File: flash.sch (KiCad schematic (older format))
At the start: 6 parts, among them U1901 MX25L1606E

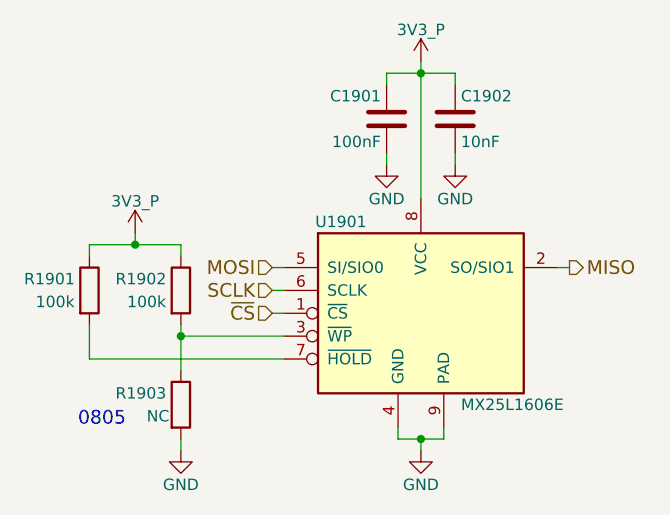
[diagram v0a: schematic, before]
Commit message: Add MIPI CSI sheet (contents need to be added once camera selection is complete)
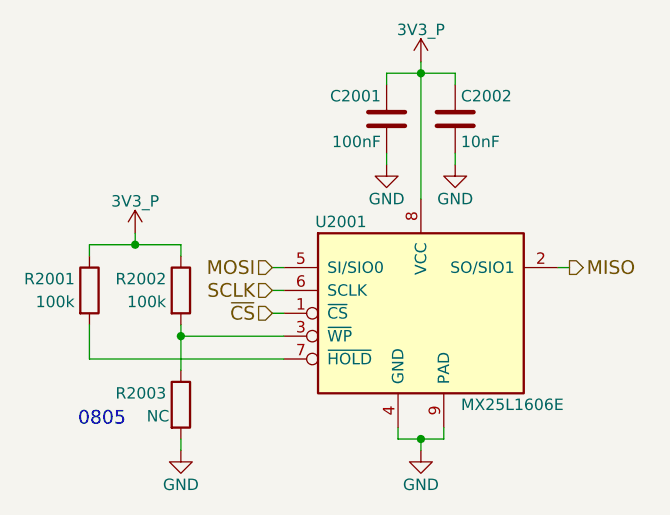
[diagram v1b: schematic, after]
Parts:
- renumbered C1901 to C2001, C1902 to C2002, R1901 to R2001, R1902 to R2002, R1903 to R2003, U1901 to U2001
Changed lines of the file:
@@
 $Descr A4 11693 8268
 encoding utf-8
-Sheet 20 20
+Sheet 20 21
 Title "SPI NOR Flash"
 Date "2018-05-18"
@@
 $EndDescr
 $Comp
-L GND #PWR0318
+L GND #PWR2005
 U 1 1 5B12CD29
 P 6000 4300
-F 0 "#PWR0318" H 6000 4050 50  0001 C CNN
+F 0 "#PWR2005" H 6000 4050 50  0001 C CNN
 F 1 "GND" H 6000 4150 50  0000 C CNN
 F 2 "" H 6000 4300 50  0001 C CNN
@@
 $EndComp
 $Comp
-L MX25L1606E U1901
+L MX25L1606E U2001
 U 1 1 5B12CFC8
 P 6000 3700
-F 0 "U1901" H 5650 4100 50  0000 C CNN
+F 0 "U2001" H 5650 4100 50  0000 C CNN
 F 1 "MX25L1606E" H 6400 3300 50  0000 C CNN
 F 2 "Housings_DFN_QFN:DFN-S-8-1EP_6x5mm_Pitch1.27mm" H 6800 3800 50  0001 C CNN
@@
 $EndComp
 $Comp
-L 3V3_P #PWR0319
+L 3V3_P #PWR2004
 U 1 1 5B12EA15
 P 6000 2600
-F 0 "#PWR0319" H 6000 2450 50  0001 C CNN
+F 0 "#PWR2004" H 6000 2450 50  0001 C CNN
 F 1 "3V3_P" H 6000 2740 50  0000 C CNN
 F 2 "" H 6000 2600 50  0001 C CNN
@@
 $EndComp
 $Comp
-L C C1901
+L C C2001
 U 1 1 5B12EA2B
 P 5850 2850
-F 0 "C1901" H 5875 2950 50  0000 L CNN
+F 0 "C2001" H 5875 2950 50  0000 L CNN
 F 1 "100nF" H 5875 2750 50  0000 L CNN
 F 2 "" H 5888 2700 50  0001 C CNN
@@
 $EndComp
 $Comp
-L C C1902
+L C C2002
 U 1 1 5B14E905
 P 6150 2850
-F 0 "C1902" H 6175 2950 50  0000 L CNN
+F 0 "C2002" H 6175 2950 50  0000 L CNN
 F 1 "10nF" H 6175 2750 50  0000 L CNN
 F 2 "" H 6188 2700 50  0001 C CNN
@@
 $EndComp
 $Comp
-L GND #PWR0320
+L GND #PWR2003
 U 1 1 5B14F686
 P 5850 3050
-F 0 "#PWR0320" H 5850 2800 50  0001 C CNN
+F 0 "#PWR2003" H 5850 2800 50  0001 C CNN
 F 1 "GND" H 5850 2900 50  0000 C CNN
 F 2 "" H 5850 3050 50  0001 C CNN
@@
 $EndComp
 $Comp
-L GND #PWR0321
+L GND #PWR2006
 U 1 1 5B14F6A1
 P 6150 3050
-F 0 "#PWR0321" H 6150 2800 50  0001 C CNN
+F 0 "#PWR2006" H 6150 2800 50  0001 C CNN
 F 1 "GND" H 6150 2900 50  0000 C CNN
 F 2 "" H 6150 3050 50  0001 C CNN
@@
 ~CS
 $Comp
-L R R1901
+L R R2001
 U 1 1 5B152CDF
 P 4550 3600
-F 0 "R1901" H 4375 3650 50  0000 C CNN
+F 0 "R2001" H 4375 3650 50  0000 C CNN
 F 1 "100k" H 4400 3550 50  0000 C CNN
 F 2 "" V 4480 3600 50  0001 C CNN
@@
 $EndComp
 $Comp
-L 3V3_P #PWR0322
+L 3V3_P #PWR2001
 U 1 1 5B152DB7
 P 4750 3350
-F 0 "#PWR0322" H 4750 3200 50  0001 C CNN
+F 0 "#PWR2001" H 4750 3200 50  0001 C CNN
 F 1 "3V3_P" H 4750 3490 50  0000 C CNN
 F 2 "" H 4750 3350 50  0001 C CNN
@@
 $EndComp
 $Comp
-L R R1902
+L R R2002
 U 1 1 5AFB92E3
 P 4950 3600
-F 0 "R1902" H 4775 3650 50  0000 C CNN
+F 0 "R2002" H 4775 3650 50  0000 C CNN
 F 1 "100k" H 4800 3550 50  0000 C CNN
 F 2 "" V 4880 3600 50  0001 C CNN
@@
 $EndComp
 $Comp
-L R R1903
+L R R2003
 U 1 1 5AFBA0EE
 P 4950 4100
-F 0 "R1903" H 4775 4150 50  0000 C CNN
+F 0 "R2003" H 4775 4150 50  0000 C CNN
 F 1 "NC" H 4850 4050 50  0000 C CNN
 F 2 "" V 4880 4100 50  0001 C CNN
@@
 Connection ~ 4950 3800
 $Comp
-L GND #PWR0323
+L GND #PWR2002
 U 1 1 5AFBA2C4
 P 4950 4300
-F 0 "#PWR0323" H 4950 4050 50  0001 C CNN
+F 0 "#PWR2002" H 4950 4050 50  0001 C CNN
 F 1 "GND" H 4950 4150 50  0000 C CNN
 F 2 "" H 4950 4300 50  0001 C CNN

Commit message: Begin assigning footprints to passive components, add component information to the common 10k resistors throughout the schematic, include TVS diodes on the switch/button I/O pins, use the DB2J20900L schottky diode throughout the design (in place of the ZLLS400)
Added notes about the battery holder, battery size, and the fact that the 103HT thermistor can fit underneath the 18650 battery when the battery is insterted into the holder.

Included frequency response curve for the new/cheaper SMD speaker (slightly thicker mechanical dimension).

Included note about the RedPine RS9116's SDIO_RESET# line expecting a 2.31V VIH logic level, increased the pull-up to 100k (M.2 standard states that this is should be 1.8V level).

Added a TODO note stating the 1.8V logic-level I2C devices should share the same level-shifter that will be on the top-level circuit (in next commit).
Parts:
- R2001, R2002, R2003: footprint (none) -> Resistors_SMD:R_0603
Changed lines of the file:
@@
 $EndDescr
 $Comp
-L GND #PWR2005
+L GND #PWR0324
 U 1 1 5B12CD29
 P 6000 4300
-F 0 "#PWR2005" H 6000 4050 50  0001 C CNN
+F 0 "#PWR0324" H 6000 4050 50  0001 C CNN
 F 1 "GND" H 6000 4150 50  0000 C CNN
 F 2 "" H 6000 4300 50  0001 C CNN
@@
 $EndComp
 $Comp
-L 3V3_P #PWR2004
+L 3V3_P #PWR0325
 U 1 1 5B12EA15
 P 6000 2600
-F 0 "#PWR2004" H 6000 2450 50  0001 C CNN
+F 0 "#PWR0325" H 6000 2450 50  0001 C CNN
 F 1 "3V3_P" H 6000 2740 50  0000 C CNN
 F 2 "" H 6000 2600 50  0001 C CNN
@@
 $EndComp
 $Comp
-L GND #PWR2003
+L GND #PWR0326
 U 1 1 5B14F686
 P 5850 3050
-F 0 "#PWR2003" H 5850 2800 50  0001 C CNN
+F 0 "#PWR0326" H 5850 2800 50  0001 C CNN
 F 1 "GND" H 5850 2900 50  0000 C CNN
 F 2 "" H 5850 3050 50  0001 C CNN
@@
 $EndComp
 $Comp
-L GND #PWR2006
+L GND #PWR0327
 U 1 1 5B14F6A1
 P 6150 3050
-F 0 "#PWR2006" H 6150 2800 50  0001 C CNN
+F 0 "#PWR0327" H 6150 2800 50  0001 C CNN
 F 1 "GND" H 6150 2900 50  0000 C CNN
 F 2 "" H 6150 3050 50  0001 C CNN
@@
 F 0 "R2001" H 4375 3650 50  0000 C CNN
 F 1 "100k" H 4400 3550 50  0000 C CNN
-F 2 "" V 4480 3600 50  0001 C CNN
+F 2 "Resistors_SMD:R_0603" V 4480 3600 50  0001 C CNN
 F 3 "" H 4550 3600 50  0001 C CNN
 	1    4550 3600
@@
 $EndComp
 $Comp
-L 3V3_P #PWR2001
+L 3V3_P #PWR0328
 U 1 1 5B152DB7
 P 4750 3350
-F 0 "#PWR2001" H 4750 3200 50  0001 C CNN
+F 0 "#PWR0328" H 4750 3200 50  0001 C CNN
 F 1 "3V3_P" H 4750 3490 50  0000 C CNN
 F 2 "" H 4750 3350 50  0001 C CNN
@@
 F 0 "R2002" H 4775 3650 50  0000 C CNN
 F 1 "100k" H 4800 3550 50  0000 C CNN
-F 2 "" V 4880 3600 50  0001 C CNN
+F 2 "Resistors_SMD:R_0603" V 4880 3600 50  0001 C CNN
 F 3 "" H 4950 3600 50  0001 C CNN
 	1    4950 3600
@@
 F 0 "R2003" H 4775 4150 50  0000 C CNN
 F 1 "NC" H 4850 4050 50  0000 C CNN
-F 2 "" V 4880 4100 50  0001 C CNN
+F 2 "Resistors_SMD:R_0603" V 4880 4100 50  0001 C CNN
 F 3 "" H 4950 4100 50  0001 C CNN
 	1    4950 4100
@@
 Connection ~ 4950 3800
 $Comp
-L GND #PWR2002
+L GND #PWR0329
 U 1 1 5AFBA2C4
 P 4950 4300
-F 0 "#PWR2002" H 4950 4050 50  0001 C CNN
+F 0 "#PWR0329" H 4950 4050 50  0001 C CNN
 F 1 "GND" H 4950 4150 50  0000 C CNN
 F 2 "" H 4950 4300 50  0001 C CNN

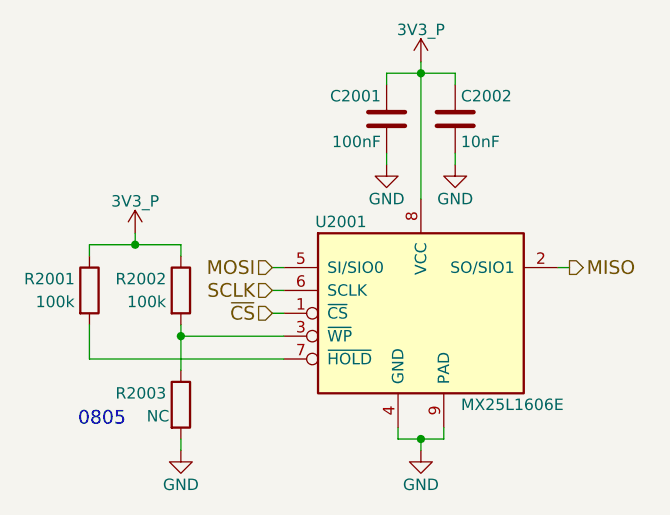
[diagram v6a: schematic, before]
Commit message: Modify the boot config/boot mode pins and switch such that only eMMC and USB (serial downloader) are boot options due to the uSD being attached to the USB<->SD bridge chip, add OV5460 notes about using the internal DVDD 1.5V regulator
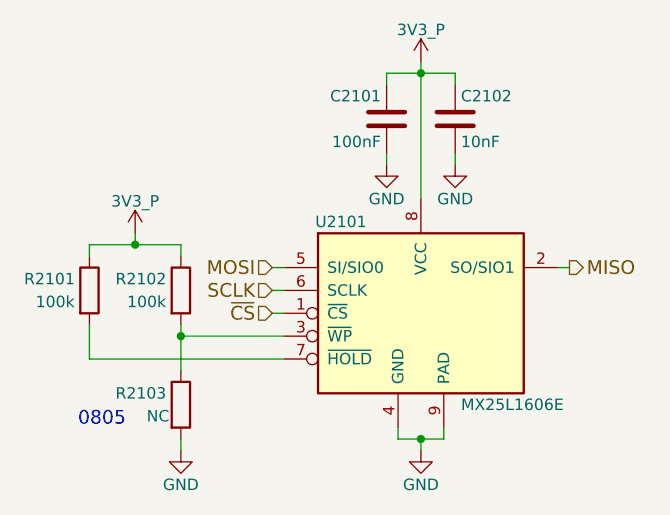
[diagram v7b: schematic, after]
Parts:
- renumbered C2001 to C2101, C2002 to C2102, R2001 to R2101, R2002 to R2102, R2003 to R2103, U2001 to U2101
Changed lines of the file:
@@
 $EndDescr
 $Comp
-L GND #PWR0327
+L GND #PWR0321
 U 1 1 5B12CD29
 P 6000 4300
-F 0 "#PWR0327" H 6000 4050 50  0001 C CNN
+F 0 "#PWR0321" H 6000 4050 50  0001 C CNN
 F 1 "GND" H 6000 4150 50  0000 C CNN
 F 2 "" H 6000 4300 50  0001 C CNN
@@
 $EndComp
 $Comp
-L MX25L1606E U2001
+L MX25L1606E U2101
 U 1 1 5B12CFC8
 P 6000 3700
-F 0 "U2001" H 5650 4100 50  0000 C CNN
+F 0 "U2101" H 5650 4100 50  0000 C CNN
 F 1 "MX25L1606E" H 6400 3300 50  0000 C CNN
 F 2 "Housings_DFN_QFN:DFN-S-8-1EP_6x5mm_Pitch1.27mm" H 6800 3800 50  0001 C CNN
@@
 $EndComp
 $Comp
-L 3V3_P #PWR0328
+L 3V3_P #PWR0322
 U 1 1 5B12EA15
 P 6000 2600
-F 0 "#PWR0328" H 6000 2450 50  0001 C CNN
+F 0 "#PWR0322" H 6000 2450 50  0001 C CNN
 F 1 "3V3_P" H 6000 2740 50  0000 C CNN
 F 2 "" H 6000 2600 50  0001 C CNN
@@
 $EndComp
 $Comp
-L C C2001
+L C C2101
 U 1 1 5B12EA2B
 P 5850 2850
-F 0 "C2001" H 5875 2950 50  0000 L CNN
+F 0 "C2101" H 5875 2950 50  0000 L CNN
 F 1 "100nF" H 5875 2750 50  0000 L CNN
 F 2 "" H 5888 2700 50  0001 C CNN
@@
 $EndComp
 $Comp
-L C C2002
+L C C2102
 U 1 1 5B14E905
 P 6150 2850
-F 0 "C2002" H 6175 2950 50  0000 L CNN
+F 0 "C2102" H 6175 2950 50  0000 L CNN
 F 1 "10nF" H 6175 2750 50  0000 L CNN
 F 2 "" H 6188 2700 50  0001 C CNN
@@
 $EndComp
 $Comp
-L GND #PWR0329
+L GND #PWR0323
 U 1 1 5B14F686
 P 5850 3050
-F 0 "#PWR0329" H 5850 2800 50  0001 C CNN
+F 0 "#PWR0323" H 5850 2800 50  0001 C CNN
 F 1 "GND" H 5850 2900 50  0000 C CNN
 F 2 "" H 5850 3050 50  0001 C CNN
@@
 $EndComp
 $Comp
-L GND #PWR0330
+L GND #PWR0324
 U 1 1 5B14F6A1
 P 6150 3050
-F 0 "#PWR0330" H 6150 2800 50  0001 C CNN
+F 0 "#PWR0324" H 6150 2800 50  0001 C CNN
 F 1 "GND" H 6150 2900 50  0000 C CNN
 F 2 "" H 6150 3050 50  0001 C CNN
@@
 ~CS
 $Comp
-L R R2001
+L R R2101
 U 1 1 5B152CDF
 P 4550 3600
-F 0 "R2001" H 4375 3650 50  0000 C CNN
+F 0 "R2101" H 4375 3650 50  0000 C CNN
 F 1 "100k" H 4400 3550 50  0000 C CNN
 F 2 "Resistors_SMD:R_0603" V 4480 3600 50  0001 C CNN
@@
 $EndComp
 $Comp
-L 3V3_P #PWR0331
+L 3V3_P #PWR0325
 U 1 1 5B152DB7
 P 4750 3350
-F 0 "#PWR0331" H 4750 3200 50  0001 C CNN
+F 0 "#PWR0325" H 4750 3200 50  0001 C CNN
 F 1 "3V3_P" H 4750 3490 50  0000 C CNN
 F 2 "" H 4750 3350 50  0001 C CNN
@@
 $EndComp
 $Comp
-L R R2002
+L R R2102
 U 1 1 5AFB92E3
 P 4950 3600
-F 0 "R2002" H 4775 3650 50  0000 C CNN
+F 0 "R2102" H 4775 3650 50  0000 C CNN
 F 1 "100k" H 4800 3550 50  0000 C CNN
 F 2 "Resistors_SMD:R_0603" V 4880 3600 50  0001 C CNN
@@
 $EndComp
 $Comp
-L R R2003
+L R R2103
 U 1 1 5AFBA0EE
 P 4950 4100
-F 0 "R2003" H 4775 4150 50  0000 C CNN
+F 0 "R2103" H 4775 4150 50  0000 C CNN
 F 1 "NC" H 4850 4050 50  0000 C CNN
 F 2 "Resistors_SMD:R_0603" V 4880 4100 50  0001 C CNN
@@
 Connection ~ 4950 3800
 $Comp
-L GND #PWR0332
+L GND #PWR0326
 U 1 1 5AFBA2C4
 P 4950 4300
-F 0 "#PWR0332" H 4950 4050 50  0001 C CNN
+F 0 "#PWR0326" H 4950 4050 50  0001 C CNN
 F 1 "GND" H 4950 4150 50  0000 C CNN
 F 2 "" H 4950 4300 50  0001 C CNN
